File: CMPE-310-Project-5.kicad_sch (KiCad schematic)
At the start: 8 parts, among them U4 8086_Min_Mode

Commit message: Update CMPE-310-Project-5.kicad_sch
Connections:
- net GND: no longer R?.2, U4.33 (MN/~{MX})
- new net: R?.2, U4.33 (MN/~{MX})
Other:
- moved on the sheet: SW?
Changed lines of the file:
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@@
   (junction (at 218.44 137.16) (diameter 0) (color 0 0 0 0)
   )
-  (junction (at 63.5 139.7) (diameter 0) (color 0 0 0 0)
-  )
   (junction (at 143.51 72.39) (diameter 0) (color 0 0 0 0)
   )
@@
   (junction (at 116.84 76.2) (diameter 0) (color 0 0 0 0)
   )
-  (junction (at 68.58 139.7) (diameter 0) (color 0 0 0 0)
-  )
   (junction (at 45.72 139.7) (diameter 0) (color 0 0 0 0)
   )
@@
     (stroke (width 0) (type default) (color 0 0 0 0))
   )
+  (wire (pts (xy 60.96 139.7) (xy 60.96 142.24))
+    (stroke (width 0) (type default) (color 0 0 0 0))
+  )
   (wire (pts (xy 114.3 121.92) (xy 119.38 121.92))
     (stroke (width 0) (type default) (color 0 0 0 0))
@@
     (stroke (width 0) (type default) (color 0 0 0 0))
   )
-  (wire (pts (xy 63.5 139.7) (xy 68.58 139.7))
-    (stroke (width 0) (type default) (color 0 0 0 0))
-  )
   (wire (pts (xy 16.51 139.7) (xy 33.02 139.7))
     (stroke (width 0) (type default) (color 0 0 0 0))
@@
     (stroke (width 0) (type default) (color 0 0 0 0))
   )
-  (wire (pts (xy 68.58 139.7) (xy 68.58 142.24))
-    (stroke (width 0) (type default) (color 0 0 0 0))
-  )
   (bus (pts (xy 267.97 41.91) (xy 267.97 58.42))
     (stroke (width 0) (type default) (color 0 0 0 0))
   )
-  (wire (pts (xy 45.72 139.7) (xy 53.34 139.7))
+  (wire (pts (xy 45.72 139.7) (xy 49.53 139.7))
     (stroke (width 0) (type default) (color 0 0 0 0))
   )
@@
     (stroke (width 0) (type default) (color 0 0 0 0))
   )
-  (wire (pts (xy 60.96 139.7) (xy 63.5 139.7))
-    (stroke (width 0) (type default) (color 0 0 0 0))
-  )
   (wire (pts (xy 218.44 139.7) (xy 222.25 139.7))
     (stroke (width 0) (type default) (color 0 0 0 0))
@@
   )
   (wire (pts (xy 114.3 81.28) (xy 119.38 81.28))
+    (stroke (width 0) (type default) (color 0 0 0 0))
+  )
+  (wire (pts (xy 59.69 139.7) (xy 60.96 139.7))
     (stroke (width 0) (type default) (color 0 0 0 0))
   )
@@
     (pin "2")
   )
+  (symbol (lib_id "power:GND") (at 60.96 142.24 0) (unit 1)
+    (in_bom yes) (on_board yes) (fields_autoplaced)
+    (property "Reference" "#PWR?" (id 0) (at 60.96 148.59 0)
+      (effects (font (size 1.27 1.27)) hide)
+    )
+    (property "Value" "" (id 1) (at 60.96 147.32 0))
+    (property "Footprint" "" (id 2) (at 60.96 142.24 0)
+      (effects (font (size 1.27 1.27)) hide)
+    )
+    (property "Datasheet" "" (id 3) (at 60.96 142.24 0)
+      (effects (font (size 1.27 1.27)) hide)
+    )
+    (pin "1")
+  )
   (symbol (lib_id "power:GND") (at 95.25 147.32 0) (unit 1)
     (in_bom yes) (on_board yes) (fields_autoplaced)
@@
     (pin "1")
   )
-  (symbol (lib_id "Switch:SW_Push") (at 58.42 139.7 0) (unit 1)
-    (in_bom yes) (on_board yes) (fields_autoplaced)
-    (property "Reference" "SW?" (id 0) (at 58.42 132.08 0))
-    (property "Value" "SW_Push" (id 1) (at 58.42 134.62 0))
-    (property "Footprint" "" (id 2) (at 58.42 134.62 0)
-      (effects (font (size 1.27 1.27)) hide)
-    )
-    (property "Datasheet" "~" (id 3) (at 58.42 134.62 0)
+  (symbol (lib_id "Switch:SW_Push") (at 54.61 139.7 0) (unit 1)
+    (in_bom yes) (on_board yes) (fields_autoplaced)
+    (property "Reference" "SW?" (id 0) (at 54.61 132.08 0))
+    (property "Value" "SW_Push" (id 1) (at 54.61 134.62 0))
+    (property "Footprint" "" (id 2) (at 54.61 134.62 0)
+      (effects (font (size 1.27 1.27)) hide)
+    )
+    (property "Datasheet" "~" (id 3) (at 54.61 134.62 0)
       (effects (font (size 1.27 1.27)) hide)
     )
@@
     )
     (property "Datasheet" "" (id 3) (at 33.02 157.48 0)
-      (effects (font (size 1.27 1.27)) hide)
-    )
-    (pin "1")
-  )
-  (symbol (lib_id "power:GND") (at 68.58 142.24 0) (unit 1)
-    (in_bom yes) (on_board yes) (fields_autoplaced)
-    (property "Reference" "#PWR?" (id 0) (at 68.58 148.59 0)
-      (effects (font (size 1.27 1.27)) hide)
-    )
-    (property "Value" "GND" (id 1) (at 68.58 147.32 0))
-    (property "Footprint" "" (id 2) (at 68.58 142.24 0)
-      (effects (font (size 1.27 1.27)) hide)
-    )
-    (property "Datasheet" "" (id 3) (at 68.58 142.24 0)
       (effects (font (size 1.27 1.27)) hide)
     )
@@
       (reference "#PWR?") (unit 1) (value "GND") (footprint "")
     )
+    (path "/30b4e89f-4c20-41a9-88b0-c155712bf13a"
+      (reference "#PWR?") (unit 1) (value "GND") (footprint "")
+    )
     (path "/3334cf2d-7196-4248-bd06-97c98423186a"
       (reference "#PWR?") (unit 1) (value "GND") (footprint "")
@@
       (reference "#PWR?") (unit 1) (value "GND") (footprint "")
     )
-    (path "/d636a63b-124b-4fe6-8a8d-b4da53029d74"
-      (reference "#PWR?") (unit 1) (value "GND") (footprint "")
-    )

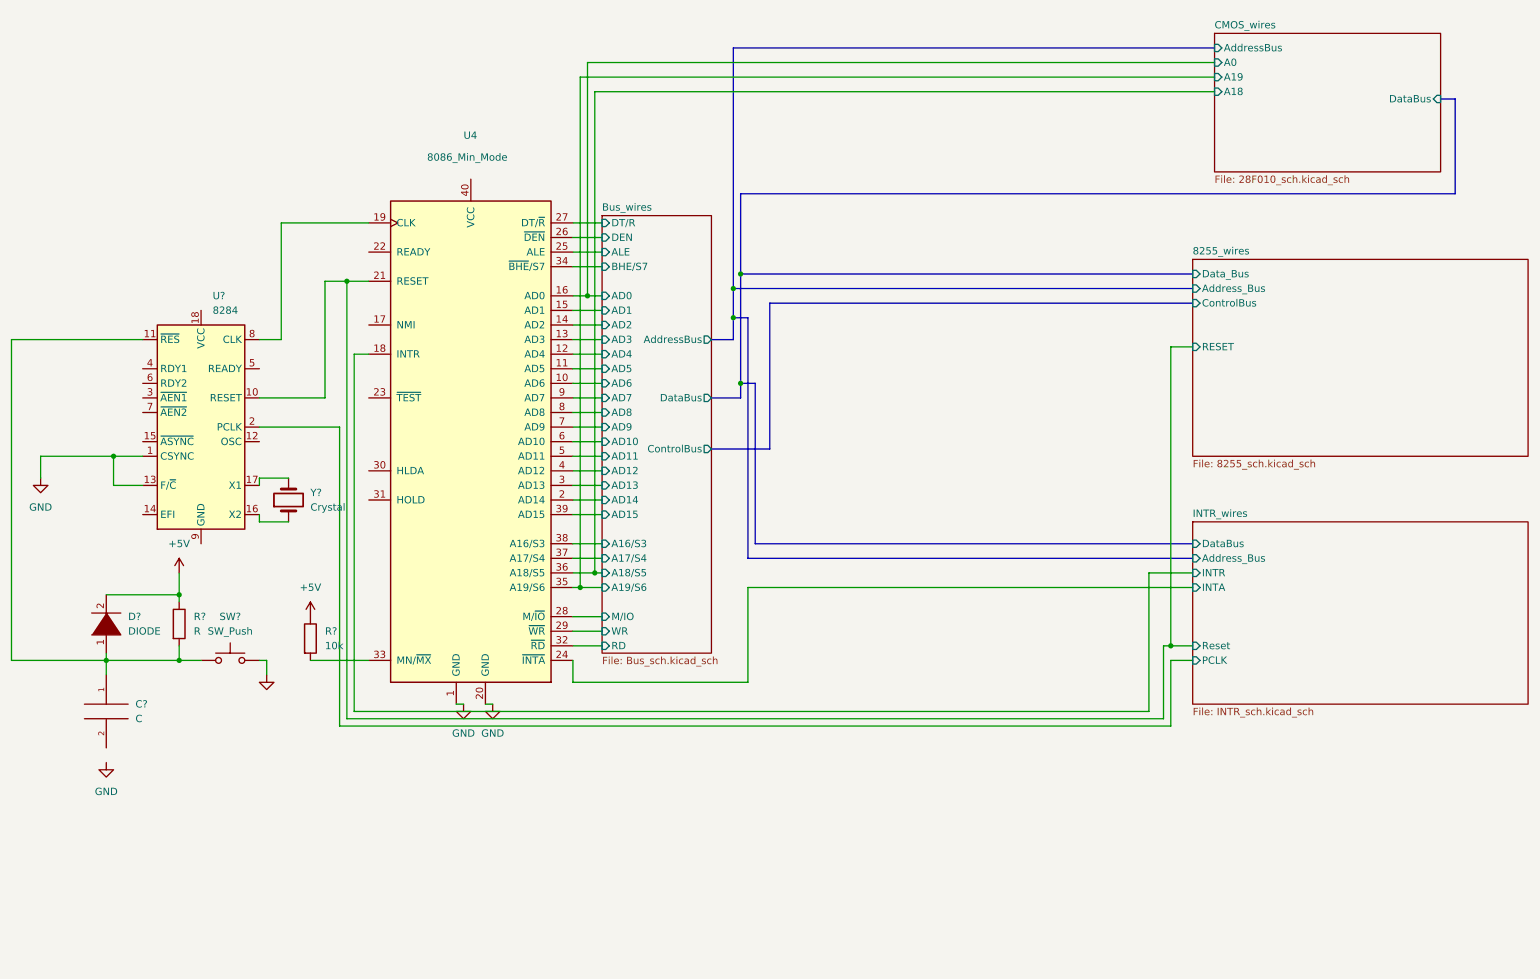
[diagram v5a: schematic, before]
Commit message: Finished wiring and decoding IO devices (except for push button switches)
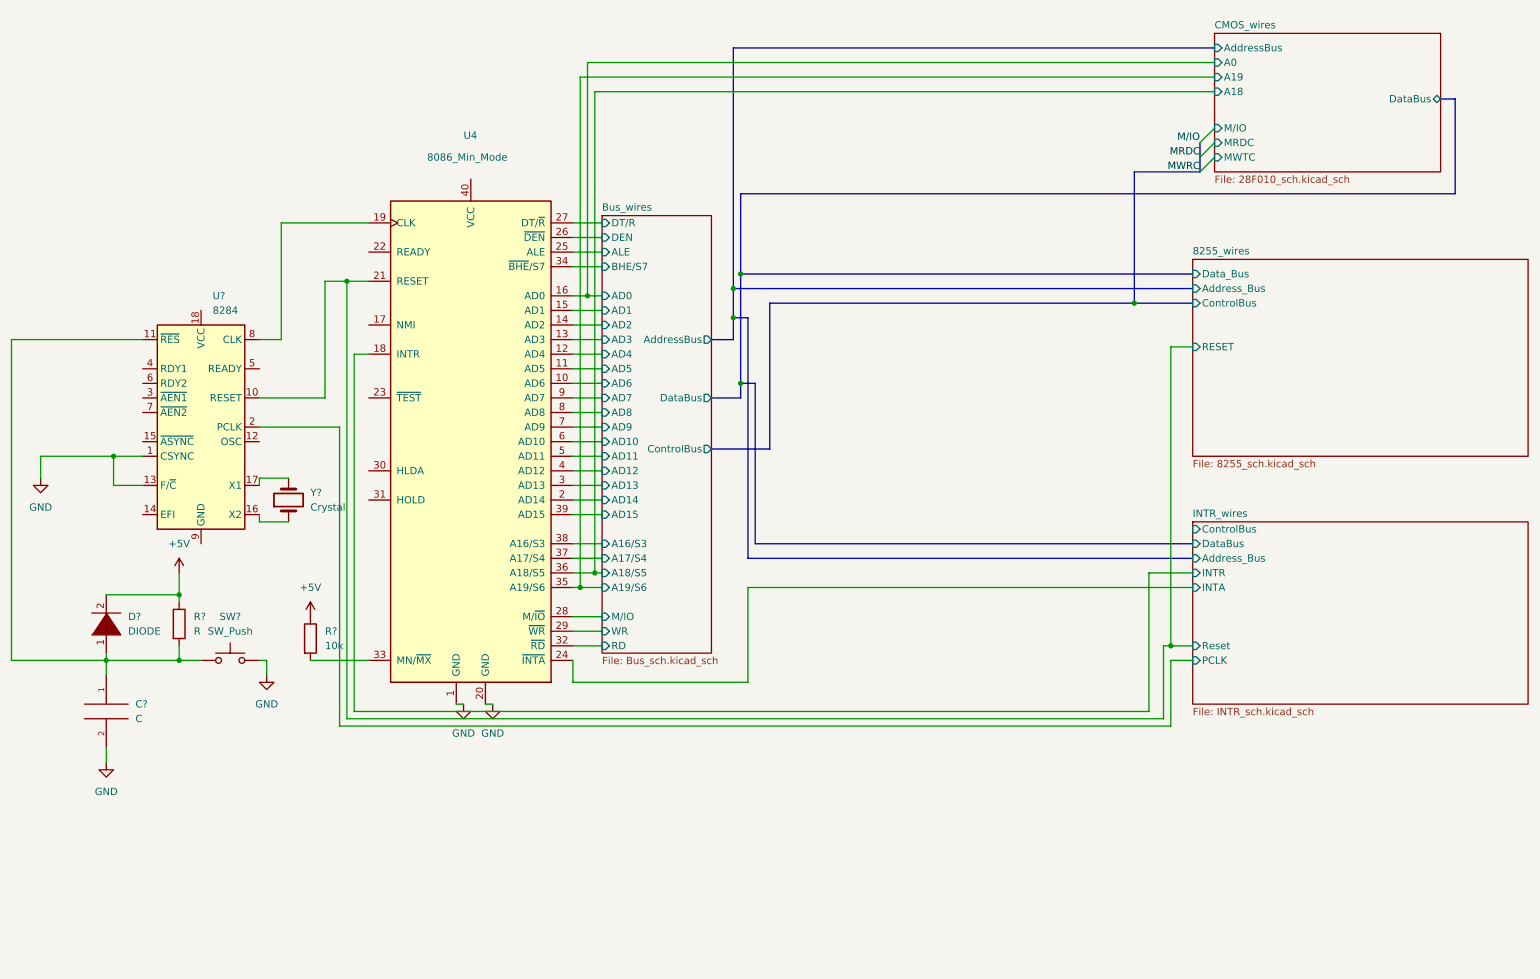
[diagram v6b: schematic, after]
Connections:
- net GND: now also C?.2
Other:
- sheet CMOS_wires ports: added MRDC, MWTC, M/IO; removed none
- sheet INTR_wires ports: added ControlBus; removed none

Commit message: Wired Push Buttons and added footprints
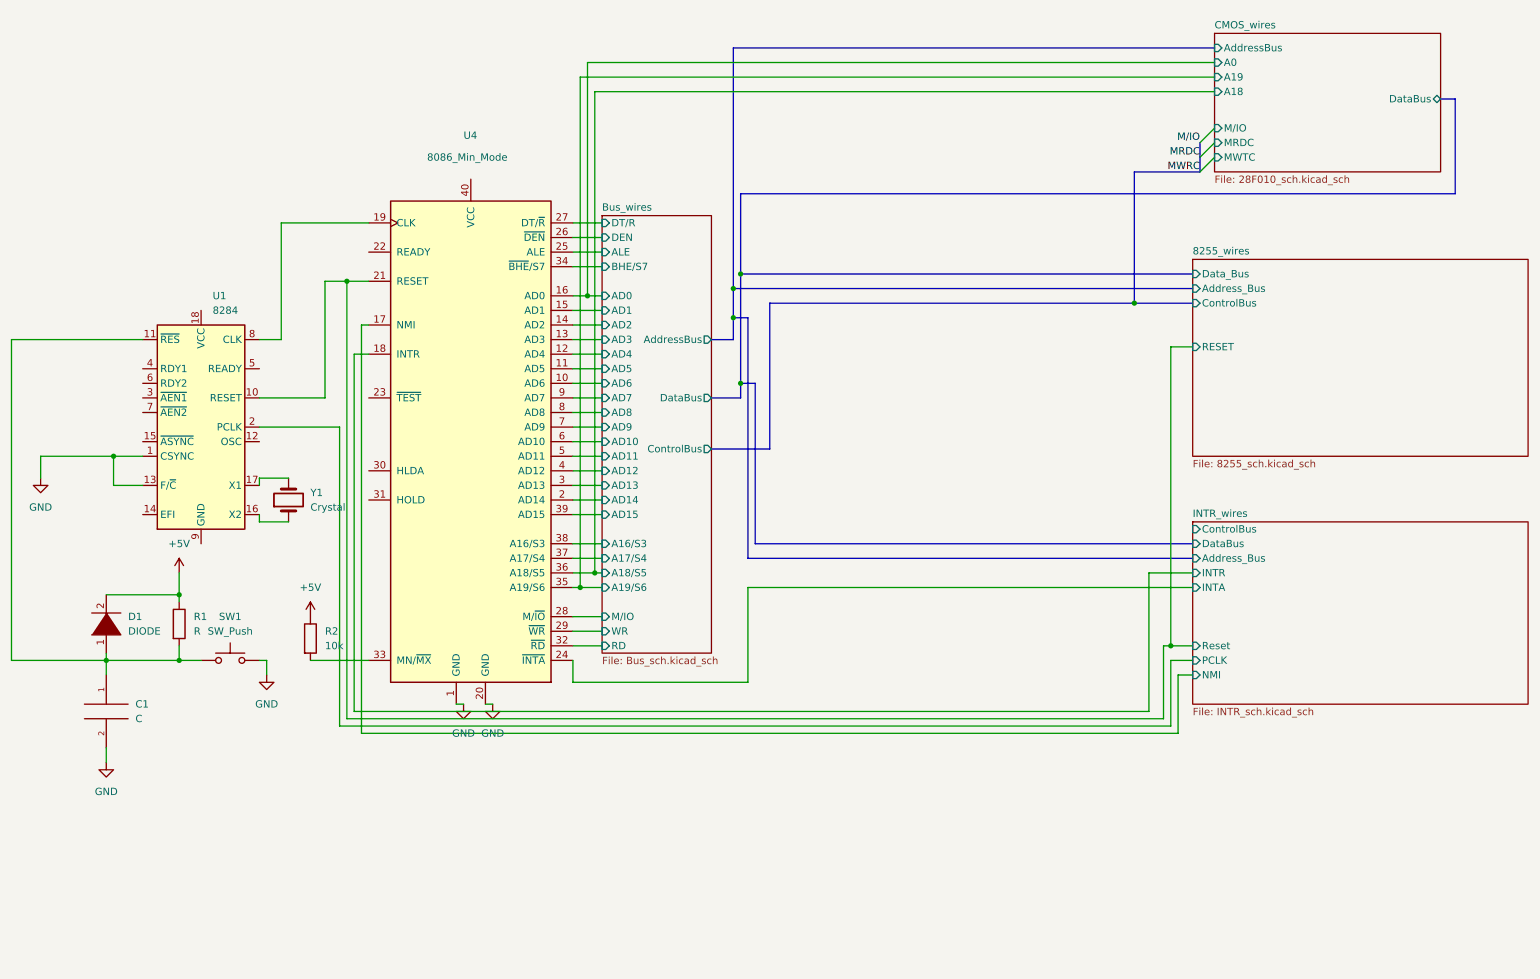
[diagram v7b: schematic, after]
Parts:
- gave numbers to parts that had none: 7
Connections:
- net INTR_wires/NMI: now reaches U4.17 (NMI)
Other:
- sheet INTR_wires ports: added NMI; removed none

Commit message: Added power and ground to chips
Added power and ground to chips as well as checked and added all labels for pins off of busses
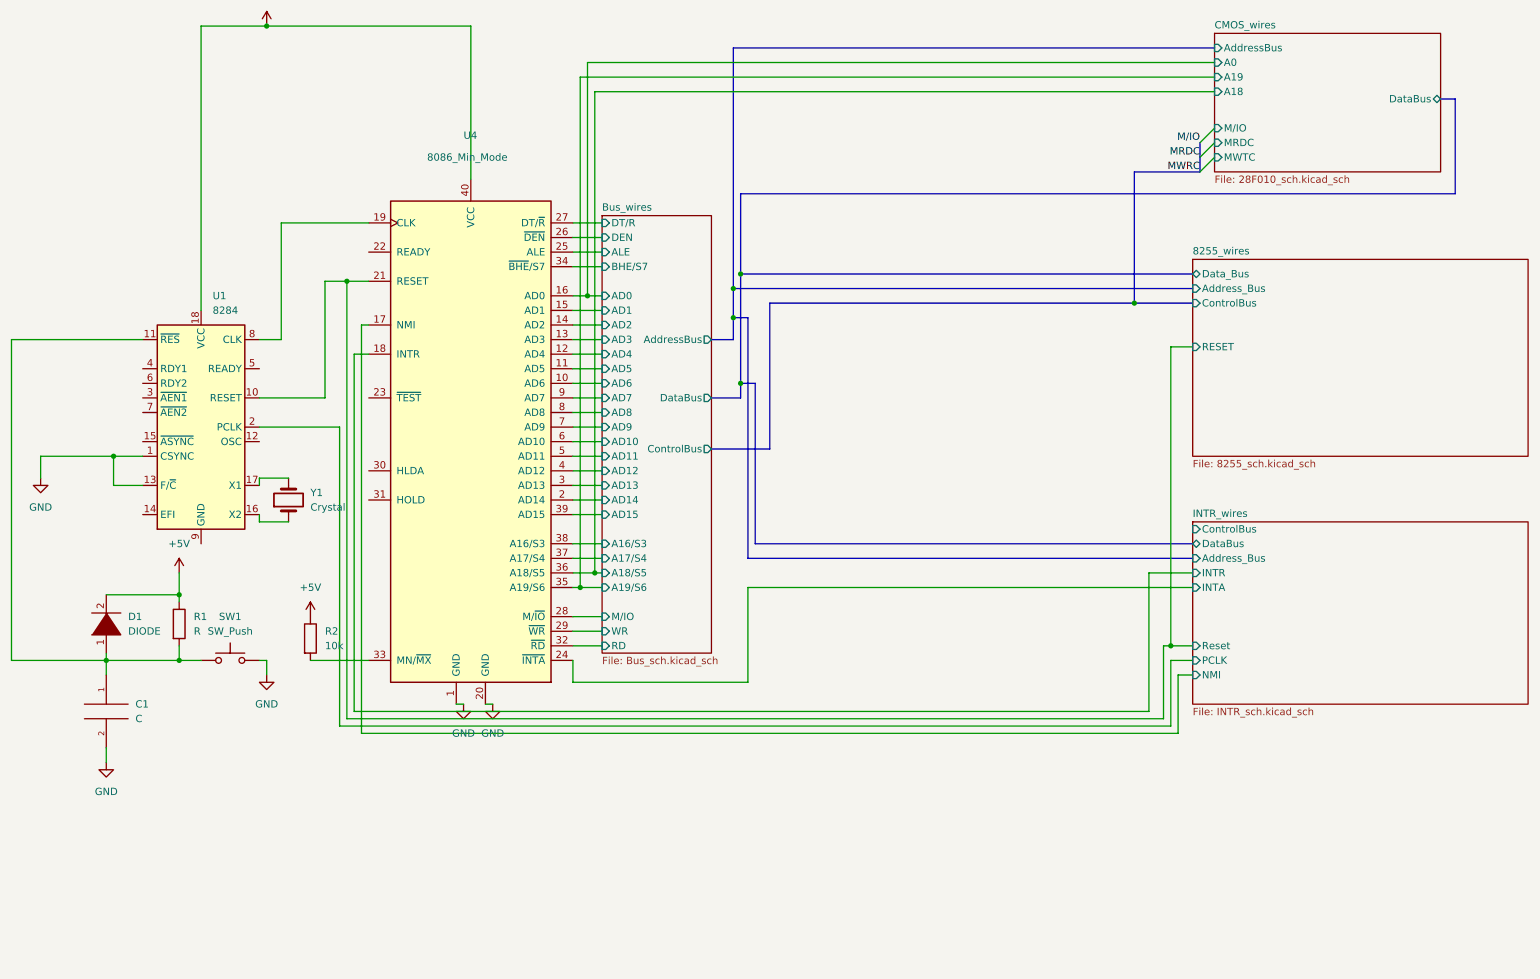
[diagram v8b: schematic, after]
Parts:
- C1: footprint (none) -> Capacitor_SMD:CP_Elec_3x5.3
- D1: footprint (none) -> Diode_SMD:D_0201_0603Metric
- R1, R2: footprint (none) -> Resistor_SMD:R_0201_0603Metric
- SW1: footprint (none) -> Button_Switch_Keyboard:SW_Cherry_MX_1.00u_PCB
- Y1: footprint (none) -> Crystal:Crystal_AT310_D3.0mm_L10.0mm_Horizontal
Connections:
- net +5V: now also U1.18 (VCC), U4.40 (VCC)
